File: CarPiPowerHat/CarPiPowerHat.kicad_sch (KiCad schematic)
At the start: 47 parts, among them J3 40HAT, J9 CONN_01X02, Q1 DMG2305UX, Q2 DMMT5401, U2 CAT24C32

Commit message: added jtag
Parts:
- added C? (x2): 100n, Capacitor_SMD:C_0402_1005Metric, symbol Device:C
- added D?: D_Dual_CommonCathode_AAK_Parallel, symbol Device:D_Dual_CommonCathode_AAK_Parallel
- added J?: Conn_02x03_Odd_Even, symbol Connector_Generic:Conn_02x03_Odd_Even
- added R?: 10K 1%, Resistor_SMD:R_0402_1005Metric, symbol Device:R
- added TP?: TestPoint, TestPoint:TestPoint_Pad_2.0x2.0mm, symbol Connector:TestPoint
- added U?: ATtiny45V-10X, Package_SO:TSSOP-8_4.4x3mm_P0.65mm, symbol MCU_Microchip_ATtiny:ATtiny45V-10X
- added U?: LM3480-5.0, Package_TO_SOT_SMD:SOT-23, symbol Regulator_Linear:LM3480-5.0
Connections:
- net +12v: no longer U?.3 (EN)
- net GND: now also C?.2, C?.2, J?.6 (Pin_6), R?.2, U?.3 (GND), U?.4 (GND)
- net P5V_HAT: now also D?.1 (K)
- new net: J?.3 (Pin_3), U?.7 (PB2)
- new net: J?.4 (Pin_4), U?.5 (AREF/PB0)
- new net: J?.5 (Pin_5), U?.1 (~RESET~/PB5)
- new net: C?.1, D?.2 (K), TP?.1, U?.1 (VO)
- new net 5V_ATTINY: D?.3 (A), J?.2 (Pin_2), U?.8 (VCC)
- new net IGN: C?.1, U?.2 (VI)
- new net PSU_EN: J?.1 (Pin_1), R?.1, U?.3 (EN), U?.6 (PB1)
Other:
- note added: "Power Control"
- note added: "The microcontroller is powered by it's own LDO when the ignition is switched on. It waits then 30 seconds for the raspberry pi to signal it is up and running. If not it will disable the power supply."
- title: Raspberry Pi HAT -> CarPi Power Hat
- moved on the sheet: C?, D?, J9, J?, L?, Q1, Q2A, Q2B, Q?, R11, R23, R24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

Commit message: Added first firmware version
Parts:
- removed C? (x4): 10u, Capacitor_SMD:C_0805_2012Metric, symbol Device:C
- removed C? (x7): 10u 35v, Capacitor_SMD:C_0805_2012Metric, symbol Device:C
- removed C?: 100uF, Capacitor_Tantalum_SMD:CP_EIA-7343-31_Kemet-D, symbol Device:CP
- removed C? (x2): nf, Capacitor_SMD:C_0402_1005Metric, symbol Device:C
- removed C? (x5): 100n, Capacitor_SMD:C_0402_1005Metric, symbol Device:C
- removed C?: 1.2nF, Capacitor_SMD:C_0402_1005Metric, symbol Device:C
- removed C?: 100n 100v, Capacitor_SMD:C_0402_1005Metric, symbol Device:C
- removed D?: D_Dual_CommonCathode_AAK_Parallel, symbol Device:D_Dual_CommonCathode_AAK_Parallel
- removed D?: MMBZ5242BLT3G, Diode_SMD:D_SOT-23_ANK, symbol Diode:BZX84Cxx
- removed J9: CONN_01X02, Connector_PinHeader_2.54mm:PinHeader_1x02_P2.54mm_Vertical, symbol Connector_Generic:Conn_01x02
- removed J?: Conn_02x03_Odd_Even, symbol Connector_Generic:Conn_02x03_Odd_Even
- removed J?: Barrel_Jack, Connector_BarrelJack:BarrelJack_Horizontal, symbol CM4IO:Barrel_Jack
- removed L?: SRN6045TA-3R3Y, Inductor_SMD:L_Bourns_SRN6045TA, symbol pspice:INDUCTOR
- removed Q1: DMG2305UX, Package_TO_SOT_SMD:SOT-23, symbol raspberrypi_hat:DMG2305UX
- removed Q2: DMMT5401, SOT-26, symbol raspberrypi_hat:DMMT5401
- removed Q?: DMP3013SFV-7, Package_SON:Diodes_PowerDI3333-8, symbol Transistor_FET:DMP3013SFV
- removed R23, R29: 10K, Resistor_SMD:R_0603_1608Metric_Pad0.84x1.00mm_HandSolder, symbol Device:R
- removed R24: 47K, Resistor_SMD:R_0603_1608Metric_Pad0.84x1.00mm_HandSolder, symbol Device:R
- removed R?: 20K 1%, Resistor_SMD:R_0402_1005Metric, symbol Device:R
- removed R?: 10R, Resistor_SMD:R_0402_1005Metric, symbol Device:R
- removed R? (x2): 12K 1%, Resistor_SMD:R_0402_1005Metric, symbol Device:R
- removed R?: 2.2K 1%, Resistor_SMD:R_0402_1005Metric, symbol Device:R
- removed R?: 10K 1%, Resistor_SMD:R_0402_1005Metric, symbol Device:R
- removed TP? (x4): TestPoint, TestPoint:TestPoint_Pad_2.0x2.0mm, symbol Connector:TestPoint
- removed U?: ATtiny45V-10X, Package_SO:TSSOP-8_4.4x3mm_P0.65mm, symbol MCU_Microchip_ATtiny:ATtiny45V-10X
- removed U?: AP64501SP-13, Package_SO:SOIC-8-1EP_3.9x4.9mm_P1.27mm_EP2.95x4.9mm_Mask2.71x3.4mm_ThermalVias, symbol CM4IO:AP64351
- removed U?: LM3480-5.0, Package_TO_SOT_SMD:SOT-23, symbol Regulator_Linear:LM3480-5.0
- added D1: LED, symbol Device:LED
- added J4: Conn_02x03_Counter_Clockwise, Connector_Molex:Molex_Mini-Fit_Jr_5569-06A1_2x03_P4.20mm_Horizontal, symbol Connector_Generic:Conn_02x03_Counter_Clockwise
- added J5: CONN_01X02, Connector_PinHeader_2.54mm:PinHeader_1x02_P2.54mm_Vertical, symbol Connector_Generic:Conn_01x02
- added R2: DNP, Resistor_SMD:R_0603_1608Metric_Pad0.84x1.00mm_HandSolder, symbol Device:R
- added R3: 10K, Resistor_SMD:R_0603_1608Metric_Pad0.84x1.00mm_HandSolder, symbol Device:R
- R11: value DNP -> 130; footprint Resistor_SMD:R_0603_1608Metric_Pad0.84x1.00mm_HandSolder -> (none)
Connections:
- net P3V3_HAT is gone; now on net +3.3v: J3.1 (P3V3)
- net +12v: now also J4.1 (Pin_1)
- net GND: now also J4.3 (Pin_3), J5.1 (Pin_1), R2.2
- net P3V3: now also R3.1; no longer U2.8 (VCC)
- net PWR_SENSE_OUT: now reaches J3.16 (BCM23)
- net PWR_SENSE_OUT: now also D1.2 (A)
- net +3.3v: now reaches J3.17 (P3V3)
- net +3.3v: now also U2.8 (VCC)
- net PWR_SENSE_IN: now reaches J3.18 (BCM24)
- net REVERSE_SENSE: now reaches J3.22 (BCM25)
- net LIGHT_SENSE: now reaches J3.24 (BCM8)
- net at U2.7 (WP): now also J5.2 (Pin_2), R2.1, R3.2; no longer R11.1
- new net: D1.1 (K), R11.1
- new net CAR_IGN: J4.5 (Pin_5)
- new net CAR_LIGHT: J4.6 (Pin_6)
- new net CAR_REVERSE: J4.2 (Pin_2)
- no-connect marks 0 -> 22
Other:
- added sheet HDMI Connectors (hdmi_connectors.kicad_sch)
- added sheet Light Input (input_pin_protect.kicad_sch)
- added sheet PSU (psu.kicad_sch)
- added sheet Power Control (power_control.kicad_sch)
- added sheet Reverse Input (input_pin_protect.kicad_sch)
- note added: "Car ignition driven power control"
- note added: "Connectors ------- HDMI for camera HDMI for display"
- note added: "LEDs"
- note added: "PSU 5V 3A"
- note added: "Raspberry Pi Hat according to sepecification"
- note removed: "+12v Input"
- note removed: "+5v @ 3A PSU ( 7.5v-28v Input )"
- note removed: "2.1mm Tip +ve"
- note removed: "5V Power Supply"
- note removed: "5V Powered HAT Protection"
- note removed: "5v @ 3A PSU"
- note removed: "Ideal diode to prevent reverse polarity at the input"
- note removed: "Power Control"
- note removed: "The microcontroller is powered by it's own LDO when the ignition is switched on. It waits then 30 seconds for the raspberry pi to signal it is up and running. If not it will disable the power supply."
- note removed: "This is based on the official Raspberry Pi spec to be able to call an extension board a HAT. https://github.com/raspberrypi/hats/blob/master/designguide.md"

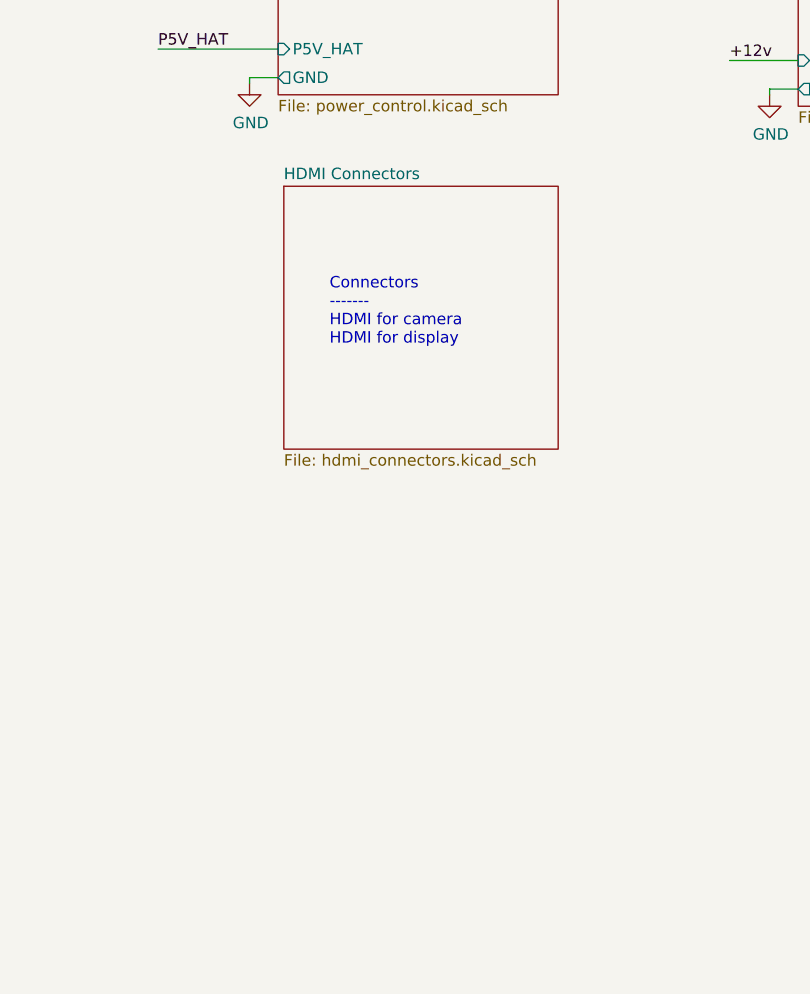
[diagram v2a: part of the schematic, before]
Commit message: added connectors
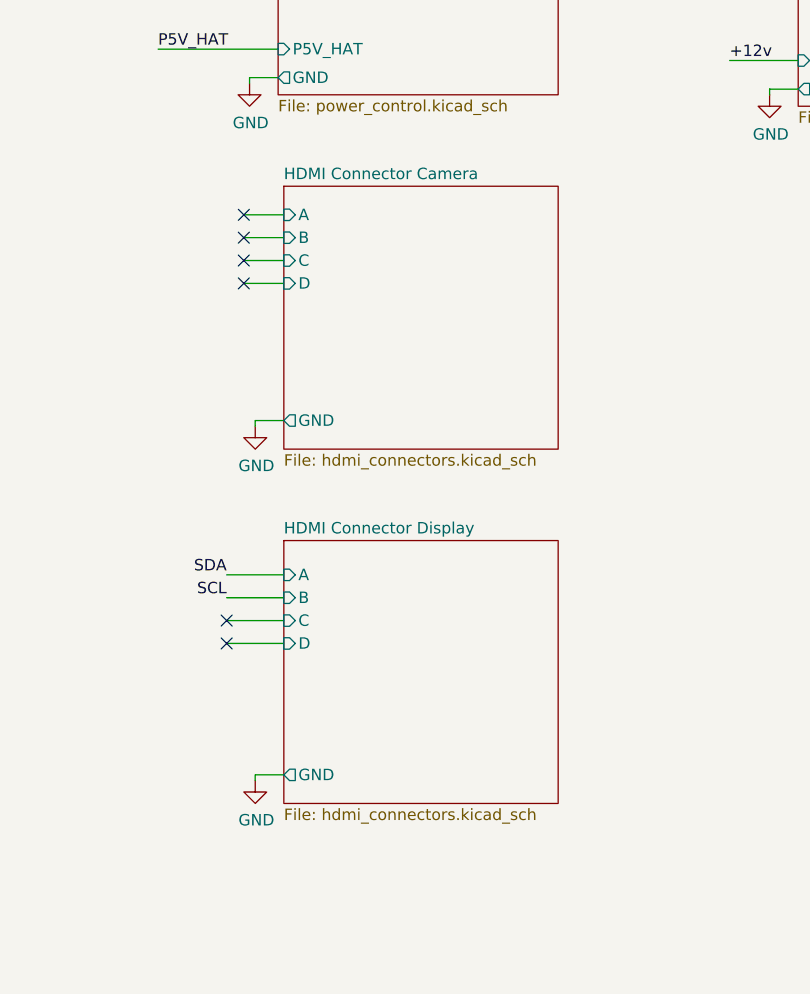
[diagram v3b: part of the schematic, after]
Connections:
- no-connect marks 22 -> 28
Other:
- sheet HDMI Connectors renamed HDMI Connector Camera
- added sheet HDMI Connector Display (hdmi_connectors.kicad_sch)
- sheet HDMI Connector Camera ports: added A, B, C, D, GND; removed none
- note removed: "Connectors ------- HDMI for camera HDMI for display"
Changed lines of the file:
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@@
   (no_connect (at 83.82 92.71))
   (no_connect (at 83.82 95.25))
+  (no_connect (at 242.57 152.4))
+  (no_connect (at 242.57 154.94))
+  (no_connect (at 244.475 107.315))
+  (no_connect (at 244.475 109.855))
+  (no_connect (at 244.475 112.395))
+  (no_connect (at 244.475 114.935))
   (wire (pts (xy 31.75 146.685) (xy 46.99 146.685))
     (stroke (width 0) (type solid) (color 0 0 0 0))
@@
     (stroke (width 0) (type solid) (color 0 0 0 0))
   )
+  (wire (pts (xy 242.57 147.32) (xy 248.92 147.32))
+    (stroke (width 0) (type solid) (color 0 0 0 0))
+  )
+  (wire (pts (xy 242.57 149.86) (xy 248.92 149.86))
+    (stroke (width 0) (type solid) (color 0 0 0 0))
+  )
+  (wire (pts (xy 242.57 152.4) (xy 248.92 152.4))
+    (stroke (width 0) (type solid) (color 0 0 0 0))
+  )
   (wire (pts (xy 243.205 29.845) (xy 248.285 29.845))
     (stroke (width 0) (type solid) (color 0 0 0 0))
@@
     (stroke (width 0) (type solid) (color 0 0 0 0))
   )
+  (wire (pts (xy 244.475 107.315) (xy 248.92 107.315))
+    (stroke (width 0) (type solid) (color 0 0 0 0))
+  )
+  (wire (pts (xy 244.475 109.855) (xy 248.92 109.855))
+    (stroke (width 0) (type solid) (color 0 0 0 0))
+  )
+  (wire (pts (xy 244.475 112.395) (xy 248.92 112.395))
+    (stroke (width 0) (type solid) (color 0 0 0 0))
+  )
+  (wire (pts (xy 244.475 114.935) (xy 248.92 114.935))
+    (stroke (width 0) (type solid) (color 0 0 0 0))
+  )
   (wire (pts (xy 245.11 38.1) (xy 245.11 38.735))
     (stroke (width 0) (type solid) (color 0 0 0 0))
@@
     (stroke (width 0) (type solid) (color 0 0 0 0))
   )
+  (wire (pts (xy 245.745 130.175) (xy 245.745 130.81))
+    (stroke (width 0) (type solid) (color 0 0 0 0))
+  )
+  (wire (pts (xy 245.745 169.545) (xy 245.745 170.18))
+    (stroke (width 0) (type solid) (color 0 0 0 0))
+  )
   (wire (pts (xy 248.285 38.1) (xy 245.11 38.1))
     (stroke (width 0) (type solid) (color 0 0 0 0))
@@
   )
   (wire (pts (xy 248.285 92.075) (xy 245.11 92.075))
+    (stroke (width 0) (type solid) (color 0 0 0 0))
+  )
+  (wire (pts (xy 248.92 130.175) (xy 245.745 130.175))
+    (stroke (width 0) (type solid) (color 0 0 0 0))
+  )
+  (wire (pts (xy 248.92 154.94) (xy 242.57 154.94))
+    (stroke (width 0) (type solid) (color 0 0 0 0))
+  )
+  (wire (pts (xy 248.92 169.545) (xy 245.745 169.545))
     (stroke (width 0) (type solid) (color 0 0 0 0))
   )
@@
     (effects (font (size 2.997 2.997) (thickness 0.5994) bold) (justify left bottom))
   )
-  (text "Connectors\n-------\nHDMI for camera\nHDMI for display\n"
-    (at 254 121.92 0)
-    (effects (font (size 1.27 1.27)) (justify left bottom))
-  )
   (text "Car ignition\ndriven power control" (at 257.175 76.2 0)
     (effects (font (size 1.27 1.27)) (justify left bottom))
@@
   (label "P5V_HAT" (at 234.95 88.9 0)
     (effects (font (size 1.27 1.27)) (justify left bottom))
+  )
+  (label "SDA" (at 242.57 147.32 180)
+    (effects (font (size 1.27 1.27)) (justify right bottom))
+  )
+  (label "SCL" (at 242.57 149.86 180)
+    (effects (font (size 1.27 1.27)) (justify right bottom))
   )
   (label "+12v" (at 298.45 90.17 0)
@@
     )
     (property "Datasheet" "" (id 3) (at 245.11 92.71 0)
+      (effects (font (size 1.27 1.27)) hide)
+    )
+    (pin "1")
+  )
+  (symbol (lib_id "power:GND") (at 245.745 130.81 0) (unit 1)
+    (in_bom yes) (on_board yes)
+    (property "Reference" "#PWR?" (id 0) (at 245.745 137.16 0)
+      (effects (font (size 1.27 1.27)) hide)
+    )
+    (property "Value" "GND" (id 1) (at 245.872 135.2042 0))
+    (property "Footprint" "" (id 2) (at 245.745 130.81 0)
+      (effects (font (size 1.27 1.27)) hide)
+    )
+    (property "Datasheet" "" (id 3) (at 245.745 130.81 0)
+      (effects (font (size 1.27 1.27)) hide)
+    )
+    (pin "1")
+  )
+  (symbol (lib_id "power:GND") (at 245.745 170.18 0) (unit 1)
+    (in_bom yes) (on_board yes)
+    (property "Reference" "#PWR?" (id 0) (at 245.745 176.53 0)
+      (effects (font (size 1.27 1.27)) hide)
+    )
+    (property "Value" "GND" (id 1) (at 245.872 174.5742 0))
+    (property "Footprint" "" (id 2) (at 245.745 170.18 0)
+      (effects (font (size 1.27 1.27)) hide)
+    )
+    (property "Datasheet" "" (id 3) (at 245.745 170.18 0)
       (effects (font (size 1.27 1.27)) hide)
     )
@@
     (stroke (width 0.001) (type solid) (color 0 0 0 0))
     (fill (color 0 0 0 0.0000))
-    (property "Sheet name" "HDMI Connectors" (id 0) (at 248.92 103.5041 0)
+    (property "Sheet name" "HDMI Connector Camera" (id 0) (at 248.92 103.5041 0)
       (effects (font (size 1.27 1.27)) (justify left bottom))
     )
     (property "Sheet file" "hdmi_connectors.kicad_sch" (id 1) (at 248.92 133.8589 0)
       (effects (font (size 1.27 1.27)) (justify left top))
+    )
+    (pin "GND" output (at 248.92 130.175 180)
+      (effects (font (size 1.27 1.27)) (justify left))
+    )
+    (pin "B" input (at 248.92 109.855 180)
+      (effects (font (size 1.27 1.27)) (justify left))
+    )
+    (pin "D" input (at 248.92 114.935 180)
+      (effects (font (size 1.27 1.27)) (justify left))
+    )
+    (pin "A" input (at 248.92 107.315 180)
+      (effects (font (size 1.27 1.27)) (justify left))
+    )
+    (pin "C" input (at 248.92 112.395 180)
+      (effects (font (size 1.27 1.27)) (justify left))
+    )
+  )
+  (sheet (at 248.92 143.51) (size 30.48 29.21)
+    (stroke (width 0.001) (type solid) (color 0 0 0 0))
+    (fill (color 0 0 0 0.0000))
+    (property "Sheet name" "HDMI Connector Display" (id 0) (at 248.92 142.8741 0)
+      (effects (font (size 1.27 1.27)) (justify left bottom))
+    )
+    (property "Sheet file" "hdmi_connectors.kicad_sch" (id 1) (at 248.92 173.2289 0)
+      (effects (font (size 1.27 1.27)) (justify left top))
+    )
+    (pin "GND" output (at 248.92 169.545 180)
+      (effects (font (size 1.27 1.27)) (justify left))
+    )
+    (pin "B" input (at 248.92 149.86 180)
+      (effects (font (size 1.27 1.27)) (justify left))
+    )
+    (pin "D" input (at 248.92 154.94 180)
+      (effects (font (size 1.27 1.27)) (justify left))
+    )
+    (pin "A" input (at 248.92 147.32 180)
+      (effects (font (size 1.27 1.27)) (justify left))
+    )
+    (pin "C" input (at 248.92 152.4 180)
+      (effects (font (size 1.27 1.27)) (justify left))
     )
   )
@@
     (path "/c779e344-5031-4f2d-bf31-77741b3c4be9/" (page "4"))
     (path "/24bd5701-0eb0-4ec6-b68f-934ea2fa56bc/" (page "5"))
+    (path "/696a3b6b-1b33-4b36-bded-7b3fb05e770a/" (page ""))
     (path "/c96310d5-5754-4cd6-8de7-7840ff32f085/" (page " "))
   )
@@
       (reference "#PWR0126") (unit 1) (value "GND") (footprint "")
     )
+    (path "/4dca8a5d-06cc-4d45-96aa-c802200e6b5c"
+      (reference "#PWR?") (unit 1) (value "GND") (footprint "")
+    )
+    (path "/9cc94b4d-ded1-4d5e-baa7-2ca8f5745978"
+      (reference "#PWR?") (unit 1) (value "GND") (footprint "")
+    )
     (path "/e3bb7c26-ab6b-4a10-8caa-57fc9cfacc7e"
       (reference "D1") (unit 1) (value "LED") (footprint "")
@@
       (reference "U2") (unit 1) (value "CAT24C32") (footprint "Package_SOIC:SOIC-8_3.9x4.9mm_P1.27mm")
     )
-    (path "/1fcb31a2-51e4-4be3-8124-9d26e186cfb4/4acde07d-2159-4fc2-98be-2357e2d7f589"
-      (reference "#PWR0105") (unit 1) (value "GND") (footprint "")
-    )
     (path "/1fcb31a2-51e4-4be3-8124-9d26e186cfb4/62ba5c12-6bc0-4c2f-9e48-78a584ddf9c1"
       (reference "#PWR0106") (unit 1) (value "GND") (footprint "")
     )
+    (path "/1fcb31a2-51e4-4be3-8124-9d26e186cfb4/1a4038d3-225b-45a9-929b-911ea9c93736"
+      (reference "#PWR?") (unit 1) (value "GND") (footprint "")
+    )
+    (path "/1fcb31a2-51e4-4be3-8124-9d26e186cfb4/553b5457-58a5-41c4-83c8-c95d99ddfa47"
+      (reference "#PWR?") (unit 1) (value "GND") (footprint "")
+    )
+    (path "/1fcb31a2-51e4-4be3-8124-9d26e186cfb4/8a35ab05-0d8f-4360-a07a-9b3a66c501e3"
+      (reference "#PWR?") (unit 1) (value "GND") (footprint "")
+    )
     (path "/1fcb31a2-51e4-4be3-8124-9d26e186cfb4/d6f246fc-9543-4b53-9a27-bdd4011ecf10"
       (reference "J1") (unit 1) (value "690-019-298-412") (footprint "project_footprints:EDAC 690-019-298-412")
     )
-    (path "/1fcb31a2-51e4-4be3-8124-9d26e186cfb4/06a2e1d6-f417-49c4-b482-f4c701fb2936"
-      (reference "J2") (unit 1) (value "690-019-298-412") (footprint "project_footprints:EDAC 690-019-298-412")
-    )
-    (path "/1fcb31a2-51e4-4be3-8124-9d26e186cfb4/9d7eaac7-6717-4016-b3dc-cac432506177"
-      (reference "J6") (unit 1) (value "Conn_01x15_Female") (footprint "")
+    (path "/1fcb31a2-51e4-4be3-8124-9d26e186cfb4/fdabd193-05b7-418b-b423-c7f9635f8ada"
+      (reference "J6") (unit 1) (value "1-84953-5") (footprint "project_footprints:1849535")
     )
     (path "/d7dab0b1-a885-42c4-b558-97d79e73318c/454a9985-443f-48e2-8597-c05a8aa0e183"
@@
       (reference "FB2") (unit 1) (value "FerriteBead") (footprint "")
     )
+    (path "/696a3b6b-1b33-4b36-bded-7b3fb05e770a/1a4038d3-225b-45a9-929b-911ea9c93736"
+      (reference "#PWR?") (unit 1) (value "GND") (footprint "")
+    )
+    (path "/696a3b6b-1b33-4b36-bded-7b3fb05e770a/553b5457-58a5-41c4-83c8-c95d99ddfa47"
+      (reference "#PWR?") (unit 1) (value "GND") (footprint "")
+    )
+    (path "/696a3b6b-1b33-4b36-bded-7b3fb05e770a/62ba5c12-6bc0-4c2f-9e48-78a584ddf9c1"
+      (reference "#PWR?") (unit 1) (value "GND") (footprint "")
+    )
+    (path "/696a3b6b-1b33-4b36-bded-7b3fb05e770a/8a35ab05-0d8f-4360-a07a-9b3a66c501e3"
+      (reference "#PWR?") (unit 1) (value "GND") (footprint "")
+    )
+    (path "/696a3b6b-1b33-4b36-bded-7b3fb05e770a/d6f246fc-9543-4b53-9a27-bdd4011ecf10"
+      (reference "J?") (unit 1) (value "690-019-298-412") (footprint "project_footprints:EDAC 690-019-298-412")
+    )
+    (path "/696a3b6b-1b33-4b36-bded-7b3fb05e770a/fdabd193-05b7-418b-b423-c7f9635f8ada"
+      (reference "J?") (unit 1) (value "1-84953-5") (footprint "project_footprints:1849535")
+    )
     (path "/c96310d5-5754-4cd6-8de7-7840ff32f085/a7aec7cf-6efd-4fec-8162-e5e3d25f683e"

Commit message: doing some traces
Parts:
- removed J5: CONN_01X02, Connector_PinHeader_2.54mm:PinHeader_1x02_P2.54mm_Vertical, symbol Connector_Generic:Conn_01x02
- added H5, H6: 3mm_Mounting_Hole, MountingHole:MountingHole_2.7mm_M2.5, symbol Mechanical:MountingHole
- D1: footprint (none) -> LED_SMD:LED_0603_1608Metric
- H1, H2, H3, H4: footprint project_footprints:NPTH_3mm_ID -> MountingHole:MountingHole_2.7mm_M2.5
- J3: symbol raspberrypi_hat:OX40HAT -> CarPiPowerHat:OX40HAT
- R11: footprint (none) -> Resistor_SMD:R_0402_1005Metric
- R2, R3, R6, R8: footprint Resistor_SMD:R_0603_1608Metric_Pad0.84x1.00mm_HandSolder -> project_footprints:R_0603_1608Metric_Pad0.84x1.00mm_HandSolder
- U2: symbol raspberrypi_hat:CAT24C32 -> CarPiPowerHat:CAT24C32
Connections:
- net P3V3 is gone; now on net +3.3v: R3.1, R6.1, R8.1
- net CAR_IGN: now also J4.2 (Pin_2); no longer J4.5 (Pin_5)
- net CAR_REVERSE: now also J4.5 (Pin_5); no longer J4.2 (Pin_2)
- net SCL: now also J3.5 (BCM3)
- net SDA: now also J3.3 (BCM2)
- net BITCLK: now reaches J3.12 (BCM18)
- net LRCLK: now reaches J3.35 (BCM19)
- net BCM16: now reaches J3.36 (BCM16)
- net DATAIN: now reaches J3.40 (BCM21)
- no-connect marks 28 -> 23
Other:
- added sheet RTC Clock (RTC.kicad_sch)
- added sheet i2s_dac (i2s_dac.kicad_sch)
- moved on the sheet: D1, J4, R11, R2

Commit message: doing some traces
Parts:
- removed D1: LED, LED_SMD:LED_0603_1608Metric, symbol Device:LED
- removed R11: 130, Resistor_SMD:R_0402_1005Metric, symbol Device:R
- added J9: Conn_01x04, Connector_PinHeader_1.00mm:PinHeader_1x04_P1.00mm_Vertical, symbol Connector_Generic:Conn_01x04
- R3: footprint project_footprints:R_0603_1608Metric_Pad0.84x1.00mm_HandSolder -> Resistor_SMD:R_0603_1608Metric; LCSC (none) -> C25804
- R6, R8: footprint project_footprints:R_0603_1608Metric_Pad0.84x1.00mm_HandSolder -> Resistor_SMD:R_0603_1608Metric; LCSC (none) -> C22978
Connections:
- net HDMI Connector Camera/A: now also J9.4 (Pin_4)
- net HDMI Connector Camera/B: now also J9.3 (Pin_3)
- net HDMI Connector Camera/C: now also J9.2 (Pin_2)
- net HDMI Connector Camera/D: now also J9.1 (Pin_1)
- no-connect marks 23 -> 19
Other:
- note added: "Conects DSI/CSI to HDMI"
- note added: "DSI/CSI to HDMI adaptor"
- note added: "PSU"
- note added: "controlled by car ignition"
- note removed: "LEDs"
